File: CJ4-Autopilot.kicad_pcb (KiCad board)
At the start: 2 copper layers, 317.5 x 50.8 mm, 74 parts, among them J1 CRS encoder, J2 FLC encoder, J3 HDG encoder, J4 ALT encoder, J5 CRS encoder, J6 USB_B_Micro, J7 Conn_01x02, SW1 FD1, SW10 ALT, SW11 YD, SW12 XFR, SW13 AP, SW14 FD2, SW15 DISC, SW16 VS encoder, SW2 VS, SW3 VNAV, SW4 FLC, SW5 NAV, SW6 BANK, SW7 HDG, SW8 APPR, SW9 BC, U1 TLC5917IN, U2 AMS1117-3.3, U3 TLC5917IN, U4 74HC165, U5 74HC165, U6 W25Q128JVS, U7 RP2040, Y1 X322512MSB4SI

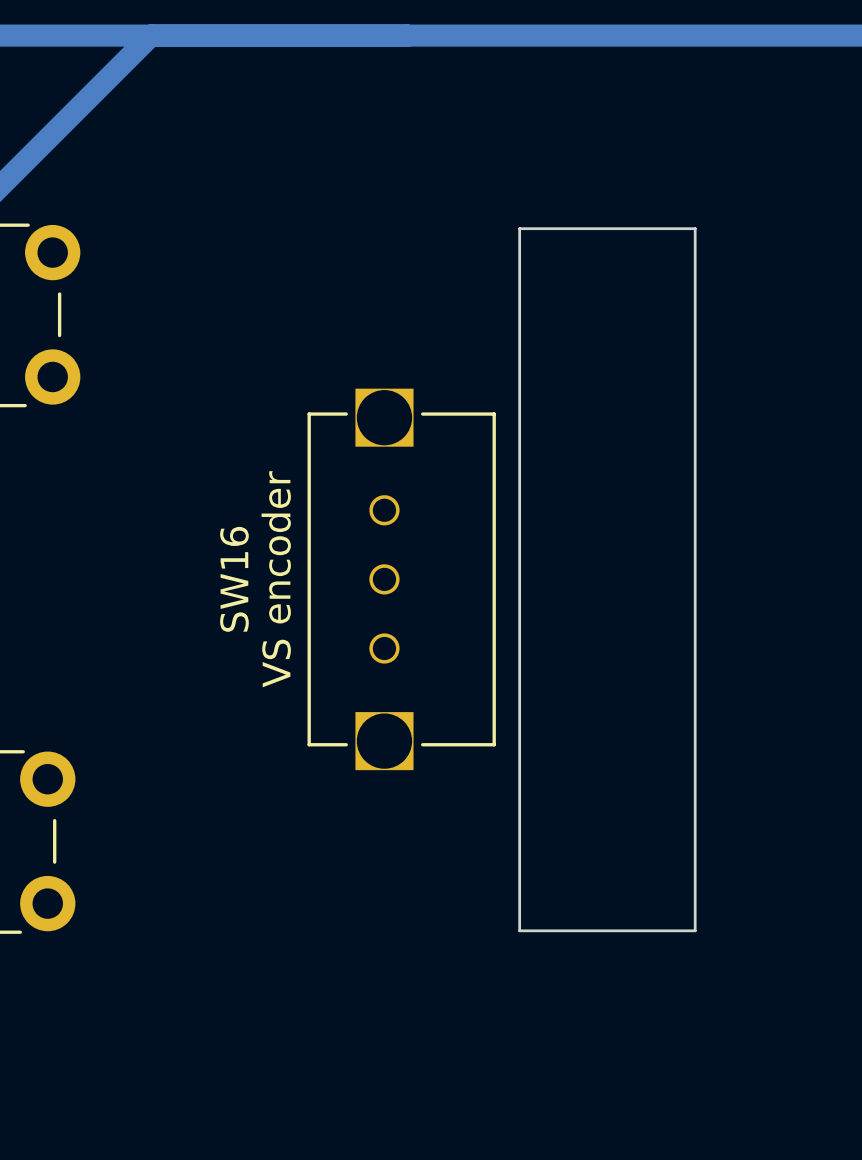
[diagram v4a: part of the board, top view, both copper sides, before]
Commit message: Add model for right angle encoder, adjust opening
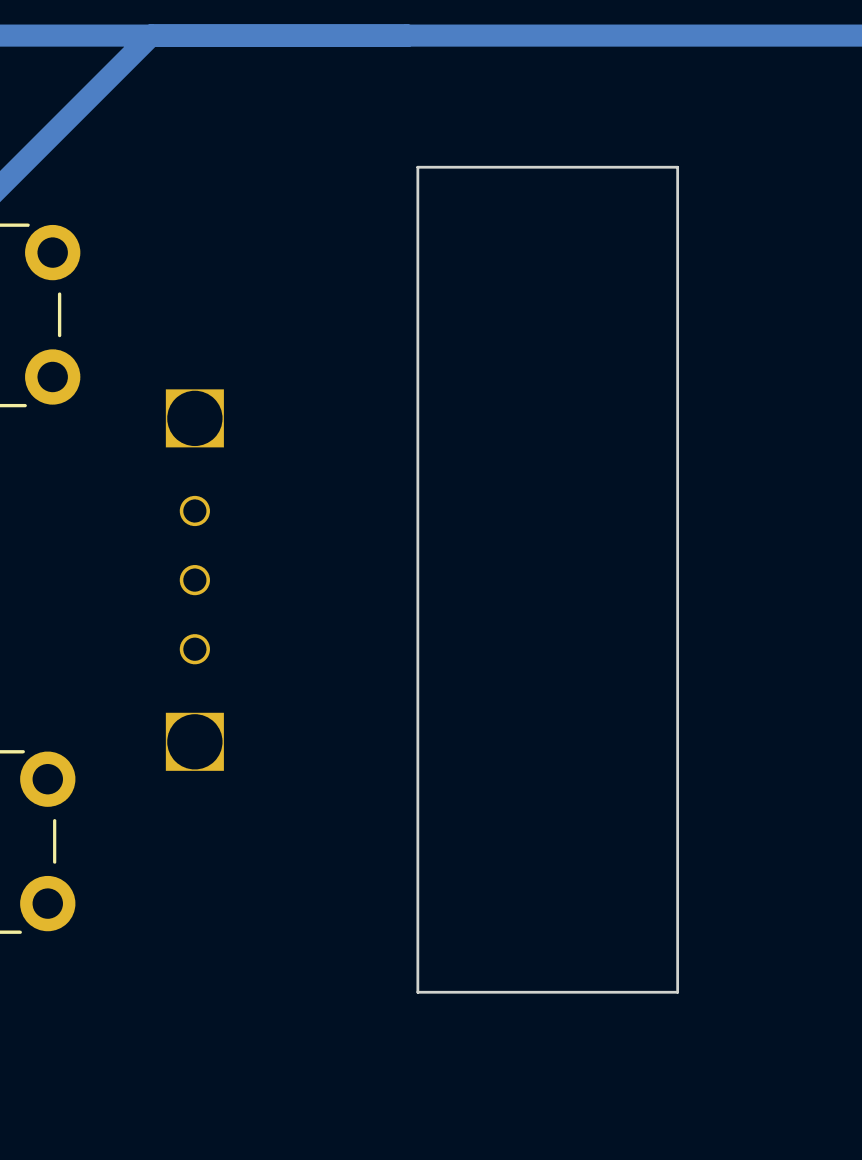
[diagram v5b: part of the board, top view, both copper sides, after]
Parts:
- SW16: moved to B.Cu
- moved SW16 6.86 mm to (80.9, 41.3), turned to -90 degrees
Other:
- outline, holes or cut-outs redrawn
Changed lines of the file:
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@@
     )
   )
-  (footprint "CJ4-Autopilot:EN11-VNB1BQ15" (layer "F.Cu")
-    (at 87.76335 41.275 90)
-    (property "Sheetfile" "CJ4-Autopilot.kicad_sch")
-    (property "Sheetname" "")
-    (attr through_hole)
-    (fp_text reference "SW16" (at 0.0127 -5.334 90) (layer "F.SilkS")
-      (effects (font (size 1 1) (thickness 0.15)))
-    )
-    (fp_text value "VS encoder" (at 0.0127 -3.81 90) (layer "F.SilkS")
-      (effects (font (size 1 1) (thickness 0.15)))
-    )
-    (fp_line (start -5.969 4.0259) (end 5.9944 4.0259) (layer "F.SilkS") (width 0.12))
-    (fp_line (start 5.9944 4.0259) (end 5.9944 1.438874) (layer "F.SilkS") (width 0.12))
-    (fp_line (start 5.9944 -2.667) (end -5.969 -2.667) (layer "F.SilkS") (width 0.12))
-    (fp_line (start -5.969 1.438874) (end -5.969 4.0259) (layer "F.SilkS") (width 0.12))
-    (fp_line (start -5.969 -2.667) (end -5.969 -1.326606) (layer "F.SilkS") (width 0.12))
-    (fp_line (start 5.9944 -1.326606) (end 5.9944 -2.667) (layer "F.SilkS") (width 0.12))
-    (fp_line (start 6.1214 10.1473) (end 6.1214 -2.794) (layer "F.CrtYd") (width 0.05))
-    (fp_line (start 6.1214 -2.794) (end -6.096 -2.794) (layer "F.CrtYd") (width 0.05))
-    (fp_line (start -6.096 10.1473) (end 6.1214 10.1473) (layer "F.CrtYd") (width 0.05))
-    (fp_line (start -6.096 -2.794) (end -6.096 10.1473) (layer "F.CrtYd") (width 0.05))
-    (fp_line (start 3.0099 3.8989) (end 3.0099 9.8933) (layer "F.Fab") (width 0.1))
-    (fp_line (start -5.842 3.8989) (end 5.8674 3.8989) (layer "F.Fab") (width 0.1))
-    (fp_line (start -2.9845 9.8933) (end 3.0099 9.8933) (layer "F.Fab") (width 0.1))
-    (fp_line (start -5.842 -2.54) (end -5.842 3.8989) (layer "F.Fab") (width 0.1))
-    (fp_line (start 5.8674 -2.54) (end -5.842 -2.54) (layer "F.Fab") (width 0.1))
-    (fp_line (start 5.8674 3.8989) (end 5.8674 -2.54) (layer "F.Fab") (width 0.1))
-    (fp_line (start -2.9845 3.8989) (end -2.9845 9.8933) (layer "F.Fab") (width 0.1))
-    (pad "" np_thru_hole rect (at -5.8373 0.056134 90) (size 2.1 2.1) (drill 2) (layers F&B.Cu *.Mask))
-    (pad "" np_thru_hole rect (at 5.8627 0.056134 90) (size 2.1 2.1) (drill 2) (layers F&B.Cu *.Mask))
-    (pad "A" thru_hole circle (at -2.4873 0.056101 90) (size 1.0922 1.0922) (drill 0.8382) (layers *.Cu *.Mask)
-      (net 47 "VS_A") (pinfunction "A") (pintype "passive"))
-    (pad "B" thru_hole circle (at 2.5127 0.056101 90) (size 1.0922 1.0922) (drill 0.8382) (layers *.Cu *.Mask)
-      (net 48 "VS_B") (pinfunction "B") (pintype "passive"))
-    (pad "C" thru_hole circle (at 0.0127 0.056101 90) (size 1.0922 1.0922) (drill 0.8382) (layers *.Cu *.Mask)
-      (net 2 "GND") (pinfunction "C") (pintype "passive"))
-  )
   (footprint "CJ4-Autopilot:JLCPCB_Tooling_Hole" (layer "F.Cu")
     (at 24.13 29.31)
@@
     )
   )
+  (footprint "CJ4-Autopilot:EN11-VNB1BQ15" (layer "B.Cu")
+    (at 80.90535 41.275 -90)
+    (property "Sheetfile" "CJ4-Autopilot.kicad_sch")
+    (property "Sheetname" "")
+    (attr through_hole)
+    (fp_text reference "SW16" (at 0.0127 5.334 90) (layer "B.SilkS")
+      (effects (font (size 1 1) (thickness 0.15)) (justify mirror))
+    )
+    (fp_text value "VS encoder" (at 0.0127 3.81 90) (layer "B.SilkS")
+      (effects (font (size 1 1) (thickness 0.15)) (justify mirror))
+    )
+    (fp_line (start -5.969 -4.0259) (end 5.9944 -4.0259) (layer "B.SilkS") (width 0.12))
+    (fp_line (start 5.9944 -4.0259) (end 5.9944 -1.438874) (layer "B.SilkS") (width 0.12))
+    (fp_line (start 5.9944 2.667) (end -5.969 2.667) (layer "B.SilkS") (width 0.12))
+    (fp_line (start -5.969 -1.438874) (end -5.969 -4.0259) (layer "B.SilkS") (width 0.12))
+    (fp_line (start -5.969 2.667) (end -5.969 1.326606) (layer "B.SilkS") (width 0.12))
+    (fp_line (start 5.9944 1.326606) (end 5.9944 2.667) (layer "B.SilkS") (width 0.12))
+    (fp_line (start 6.1214 -10.1473) (end 6.1214 2.794) (layer "B.CrtYd") (width 0.05))
+    (fp_line (start 6.1214 2.794) (end -6.096 2.794) (layer "B.CrtYd") (width 0.05))
+    (fp_line (start -6.096 -10.1473) (end 6.1214 -10.1473) (layer "B.CrtYd") (width 0.05))
+    (fp_line (start -6.096 2.794) (end -6.096 -10.1473) (layer "B.CrtYd") (width 0.05))
+    (fp_line (start 3.0099 -3.8989) (end 3.0099 -9.8933) (layer "B.Fab") (width 0.1))
+    (fp_line (start -5.842 -3.8989) (end 5.8674 -3.8989) (layer "B.Fab") (width 0.1))
+    (fp_line (start -2.9845 -9.8933) (end 3.0099 -9.8933) (layer "B.Fab") (width 0.1))
+    (fp_line (start -5.842 2.54) (end -5.842 -3.8989) (layer "B.Fab") (width 0.1))
+    (fp_line (start 5.8674 2.54) (end -5.842 2.54) (layer "B.Fab") (width 0.1))
+    (fp_line (start 5.8674 -3.8989) (end 5.8674 2.54) (layer "B.Fab") (width 0.1))
+    (fp_line (start -2.9845 -3.8989) (end -2.9845 -9.8933) (layer "B.Fab") (width 0.1))
+    (pad "" np_thru_hole rect (at -5.8373 -0.056134 270) (size 2.1 2.1) (drill 2) (layers F&B.Cu *.Mask))
+    (pad "" np_thru_hole rect (at 5.8627 -0.056134 270) (size 2.1 2.1) (drill 2) (layers F&B.Cu *.Mask))
+    (pad "A" thru_hole circle (at -2.4873 -0.056101 270) (size 1.0922 1.0922) (drill 0.8382) (layers *.Cu *.Mask)
+      (net 47 "VS_A") (pinfunction "A") (pintype "passive"))
+    (pad "B" thru_hole circle (at 2.5127 -0.056101 270) (size 1.0922 1.0922) (drill 0.8382) (layers *.Cu *.Mask)
+      (net 48 "VS_B") (pinfunction "B") (pintype "passive"))
+    (pad "C" thru_hole circle (at 0.0127 -0.056101 270) (size 1.0922 1.0922) (drill 0.8382) (layers *.Cu *.Mask)
+      (net 2 "GND") (pinfunction "C") (pintype "passive"))
+    (model "${KIPRJMOD}/3D Models/Right angle encoder.step"
+      (offset (xyz 0 2.54 0))
+      (scale (xyz 1 1 1))
+      (rotate (xyz 0 0 90))
+    )
+  )
   (footprint "CJ4-Autopilot:Perfect_0402" (layer "B.Cu")
     (at 129.54 52.748705 -90)
@@
   (gr_arc (start 19.05 21.59) (mid 19.793949 19.793949) (end 21.59 19.05) (layer "Edge.Cuts") (width 0.1))
   (gr_arc (start 334.01 19.05) (mid 335.806051 19.793949) (end 336.55 21.59) (layer "Edge.Cuts") (width 0.1))
-  (gr_rect (start 92.71 28.575) (end 99.06 53.975) (layer "Edge.Cuts") (width 0.1) (fill none))
+  (gr_rect (start 89.027 26.3525) (end 98.425 56.1975) (layer "Edge.Cuts") (width 0.1) (fill none))
   (gr_line (start 19.05 21.59) (end 19.05 67.945) (layer "Edge.Cuts") (width 0.1))
   (gr_line (start 21.59 19.05) (end 334.01 19.05) (layer "Edge.Cuts") (width 0.1))

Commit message: All power routed???
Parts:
- moved C4 3.57 mm to (52.1, 54.4)
- moved C1 3.44 mm to (51.4, 35.1), turned to -90 degrees
- moved C3 3.30 mm to (290.8, 54.1)
- moved C2 1.78 mm to (290.8, 33.5)
- moved R2 1.14 mm to (55.1, 36.8), turned to 0 degrees
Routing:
- net +3V3: track 28.5 -> 374.1 mm, vias 0 -> 13
- net VBUS: track 385.8 -> 412.8 mm, vias 0 -> 9
- net GND: track 27.1 -> 41.6 mm, vias 22 -> 31
- net YD: track 0.00 -> 7.33 mm
- net XFR: track 0.00 -> 7.33 mm
- net VS: track 0.00 -> 7.33 mm
- net VNAV: track 0.00 -> 7.33 mm
- net NAV: track 0.00 -> 7.33 mm
- net HDG: track 0.00 -> 7.33 mm
- net FLC: track 0.00 -> 7.33 mm
- net FD2: track 0.00 -> 7.33 mm
- net FD1: track 0.00 -> 7.33 mm
- net BC: track 0.00 -> 7.33 mm
- net BANK: track 0.00 -> 7.33 mm
- net APPR: track 0.00 -> 7.33 mm
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
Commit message: Moved chips, rotated encoder. Lots of traces, it's gonna work!
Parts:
- added H10: VS encoder, MountingHole:MountingHole_3.2mm_M3, F.Cu at (102.1, 30.0)
- added H11: VS encoder, MountingHole:MountingHole_3.2mm_M3, F.Cu at (102.1, 52.8)
- moved R2 246.0 mm to (301.0, 27.2)
- moved U3 239.4 mm to (297.2, 31.8), turned to 90 degrees
- moved RN4 238.9 mm to (296.9, 57.4), turned to 90 degrees
- moved U5 238.8 mm to (297.2, 50.5), turned to 90 degrees
- moved RN1 135.7 mm to (162.2, 42.9), turned to -90 degrees
- moved U1 135.0 mm to (162.2, 31.7), turned to 90 degrees
- moved U4 135.0 mm to (162.2, 50.7), turned to 90 degrees
- moved R1 128.0 mm to (165.7, 27.1), turned to 0 degrees
- moved C1 117.8 mm to (169.0, 28.6), turned to 0 degrees
- moved C4 117.1 mm to (169.0, 47.9), turned to 0 degrees
- moved RN2 103.8 mm to (162.2, 57.3), turned to 90 degrees
- moved SW16 21.6 mm to (102.5, 41.5), turned to 90 degrees
- moved C3 14.9 mm to (304.3, 47.8), turned to 0 degrees
- moved C2 13.1 mm to (303.5, 30.3), turned to -90 degrees
- renumbered H10 to H12, H11 to H13, H12 to H14
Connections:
- net Net-(U1-Pad14) renamed /SDO
- RN1 pad 5: FLC -> VNAV
- RN1 pad 6: VNAV -> FLC
- U1 pad 10: BANK_LED -> VNAV_LED
- U1 pad 11: HDG_LED -> VS_LED
- U1 pad 12: APPR_LED -> FLC_LED
- U1 pad 5: FD1_LED -> NAV_LED
- U1 pad 6: VS_LED -> BANK_LED
- U1 pad 7: VNAV_LED -> HDG_LED
- U1 pad 8: FLC_LED -> APPR_LED
- U1 pad 9: NAV_LED -> FD1_LED
- U4 pad 13: VNAV -> FLC
- U4 pad 14: FLC -> VNAV
- U7 pad 15: VS_A -> /RP2040/GPIO12
- U7 pad 16: VS_B -> /RP2040/GPIO13
- U7 pad 2: CRS1_BTN -> /RP2040/GPIO00
- U7 pad 29: BTN_CLOCK -> /RP2040/GPIO18
- U7 pad 30: BTN_LATCH -> /RP2040/GPIO19
- U7 pad 31: BTN_DATA -> /RP2040/GPIO20
- U7 pad 32: LED_DATA -> /RP2040/GPIO21
- U7 pad 34: LED_CLOCK -> FLC_BTN
- U7 pad 35: LED_LATCH -> FLC_B
- U7 pad 36: FLC_BTN -> FLC_A
- U7 pad 37: /RP2040/GPIO25 -> CRS1_BTN
- U7 pad 38: /RP2040/GPIO26 -> CRS1_B
- U7 pad 39: /RP2040/GPIO27 -> CRS1_A
- U7 pad 40: /RP2040/GPIO28 -> VS_A
- U7 pad 41: /RP2040/GPIO29 -> VS_B
- U7 pad 6: CRS1_A -> /RP2040/GPIO04
- U7 pad 7: CRS1_B -> /RP2040/GPIO05
- U7 pad 8: FLC_A -> /RP2040/GPIO06
- U7 pad 9: FLC_B -> /RP2040/GPIO07
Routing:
- net CRS2_BTN: track 0.00 -> 153.1 mm
- net CRS2_B: track 0.00 -> 150.4 mm
- net CRS2_A: track 0.00 -> 146.9 mm
- net FD1_LED: track 0.00 -> 125.8 mm, vias 0 -> 1
- net FD1: track 7.33 -> 132.3 mm, vias 0 -> 1
- net CRS1_A: track 0.00 -> 101.1 mm
- net VS_LED: track 0.00 -> 96.9 mm, vias 0 -> 1
- net CRS1_B: track 0.00 -> 95.9 mm
- net CRS1_BTN: track 0.00 -> 93.3 mm
- net VS: track 7.33 -> 99.9 mm, vias 0 -> 1
- net ALT_A: track 0.00 -> 82.9 mm
- net VNAV: track 7.33 -> 89.5 mm, vias 0 -> 1
- net VNAV_LED: track 0.00 -> 81.5 mm, vias 0 -> 1
- net ALT_B: track 0.00 -> 78.2 mm
- net ALT_BTN: track 0.00 -> 70.5 mm
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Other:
- outline, holes or cut-outs redrawn

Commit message: Left side fully connected
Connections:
- RN1 pad 5: VNAV -> /Input shifter/D3
- RN1 pad 6: FLC -> /Input shifter/D2
- RN1 pad 7: VS -> /Input shifter/D1
- RN1 pad 8: FD1 -> /Input shifter/D0
- U4 pad 11: FD1 -> /Input shifter/D0
- U4 pad 12: VS -> /Input shifter/D1
- U4 pad 13: FLC -> /Input shifter/D2
- U4 pad 14: VNAV -> /Input shifter/D3
- U7 pad 11: HDG_A -> SPEED_BTN
- U7 pad 12: HDG_B -> CRS2_BTN
- U7 pad 13: CRS2_A -> CRS2_B
- U7 pad 14: CRS2_B -> CRS2_A
- U7 pad 15: /RP2040/GPIO12 -> ALT_BTN
- U7 pad 16: /RP2040/GPIO13 -> ALT_B
- U7 pad 18: ALT_B -> HDG_BTN
- U7 pad 27: ALT_BTN -> HDG_A
- U7 pad 28: BACKLIGHT_BRIGHT -> HDG_B
- U7 pad 29: /RP2040/GPIO18 -> FLC_BTN
- U7 pad 3: SPEED_BTN -> /RP2040/GPIO01
- U7 pad 30: /RP2040/GPIO19 -> FLC_B
- U7 pad 31: /RP2040/GPIO20 -> FLC_A
- U7 pad 32: /RP2040/GPIO21 -> CRS1_BTN
- U7 pad 34: FLC_BTN -> CRS1_B
- U7 pad 35: FLC_B -> CRS1_A
- U7 pad 36: FLC_A -> VNAV
- U7 pad 37: CRS1_BTN -> VS_A
- U7 pad 38: CRS1_B -> VS_B
- U7 pad 39: CRS1_A -> VS
- U7 pad 4: CRS2_BTN -> /RP2040/GPIO02
- U7 pad 40: VS_A -> FD1
- U7 pad 41: VS_B -> FLC
- U7 pad 5: HDG_BTN -> /RP2040/GPIO03
- U7 pad 6: /RP2040/GPIO04 -> LED_CLOCK
- U7 pad 7: /RP2040/GPIO05 -> LED_LATCH
- U7 pad 9: /RP2040/GPIO07 -> LED_DATA
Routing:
- net FLC: track 63.5 -> 24.1 mm, vias 1 -> 0
- net ALT_BTN: track 70.5 -> 109.6 mm
- net CRS2_B: track 150.4 -> 184.6 mm
- net CRS2_BTN: track 153.1 -> 186.9 mm
- net HDG_B: track 34.1 -> 67.6 mm
- net CRS2_A: track 146.9 -> 179.7 mm
- net HDG_A: track 28.4 -> 61.1 mm
- net ALT_B: track 78.2 -> 108.1 mm
- net FD1: track 132.3 -> 103.9 mm, vias 1 -> 2
- net VS: track 99.9 -> 75.6 mm, vias 1 -> 0
- net ALT_A: track 82.9 -> 103.6 mm
- net HDG_BTN: track 36.9 -> 55.7 mm
- net VNAV_LED: track 81.5 -> 100.1 mm, vias 1 -> 2
- net VNAV: track 89.5 -> 71.0 mm, vias 1 -> 0
- net FD1_LED: track 125.8 -> 141.5 mm, vias 1 -> 2
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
